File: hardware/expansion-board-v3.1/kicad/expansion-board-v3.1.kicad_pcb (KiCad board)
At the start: 6 copper layers, 100 x 62 mm, 156 parts, among them J1 PinHeader_2x20_P2.54mm_Vertic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, J2 U.FL_Hirose_U.FL-R-SMT-1_Vert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, J4 USB_C_Receptacle_HRO_TYPE-C-3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, J5 U.FL_Hirose_U.FL-R-SMT-1_Vert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, J6 U.FL_Hirose_U.FL-R-SMT-1_Vert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, J8 U.FL_Hirose_U.FL-R-SMT-1_Vert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, Q2 SOT-23, Q3 SOT-23, Q4 SOT-23, Q5 SOT-23, SW1 SolderJumper-2_P1.3mm_Open_Pa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, SW2 SolderJumper-2_P1.3mm_Open_Pa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, U1 SOT-23-5, U10 QFN-48-1EP_7x7mm_P0.5mm_EP5.1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, U11 DFN-8-1EP_2x2mm_P0.5mm_EP0.86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, U12 SOT-363_SC-70-6, U13 AD8319_LFCSP-8-EP, U14 MSOP-8_3x3mm_P0.65mm, U15 SOT-23-6, U16 SOT-363_SC-70-6, U17 SOT-363_SC-70-6, U2 SOT-23-5, U3 SOT-23-5, U4 BNO085_LGA-28, U5 BMP388_LGA-10, U6 LGA-16_3x3mm_P0.5mm, U7 ATGM336H_LCC-18, U8 QFN-56-1EP_7x7mm_P0.4mm_EP3.2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, U9 SOIC-8_5.3x5.3mm_P1.27mm, Y1 Crystal_SMD_3225-4Pin_3.2x2.5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, Y2 Crystal_SMD_3225-4Pin_3.2x2.5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, Y3 Crystal_SMD_3215-2Pin_3.2x1.5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

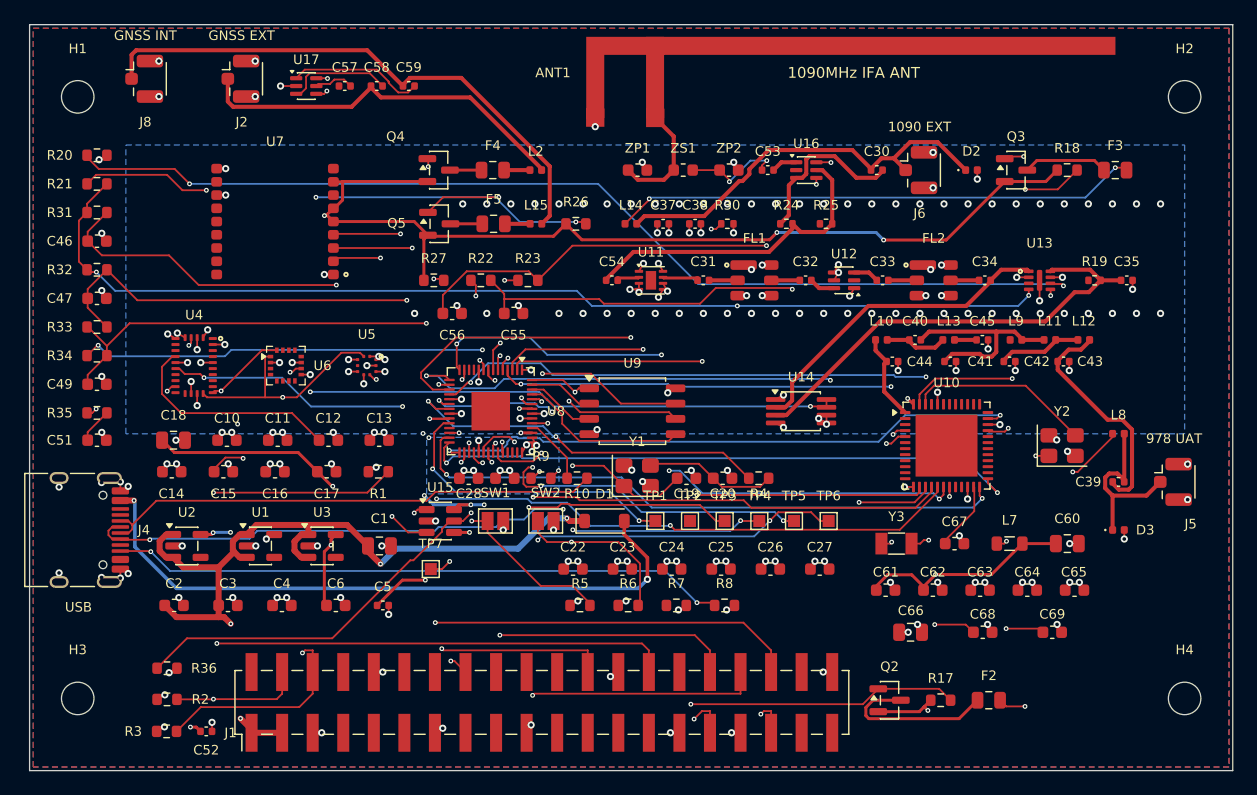
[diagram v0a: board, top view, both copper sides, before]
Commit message: feat(hw): 两脚元件按"最近引脚"定朝向——真缺线 12→4，RF 残线 6→2
评审看图指出的：很多问题不是走线本身，是 L/C 摆放时两个脚的朝向根本没考虑要连
到哪儿去，"很随意就摆了"。结果本该最短的连接反而绕远，还把旁边通道堵死。

查证属实：PLACEMENT.py 里几乎所有 0402 都是 0°，从来没排过朝向。

## orient_opt.py

两脚无极性件（R/L/C）转 180° 电气上等价，但朝向决定走线是短直还是绕过元件本体
再拐回来。判据就是"最近引脚"：

    当前成本 = |pin1 → net1 最近的外部焊盘| + |pin2 → net2 最近的外部焊盘|
    翻转成本 = |pin2位 → net1 最近点|      + |pin1位 → net2 最近点|

只动 ^[RLC]\d+$，二极管等有极性件一律跳过。两脚都是覆铜网（GND/3V3_*/RP_1V1）的
也跳过——那些靠就近过孔入平面，朝向无所谓，算出来的收益是噪声。

选中 25 个，合计省 31.6mm 连线。收益最大的 R21(AD8313_VOUT/RF_DET_OUT) 2.10mm、
R34 2.09mm、C30(ANT1090_EXT/SW1_J2) 1.92mm——C30/C59/R25 正是评审圈出来的那几个。

apply 逐行改 + 断言改了几条，不用大正则套整个文件（PLACEMENT 行内空白对齐不统一，
正则一复杂就静默漏改，项目里栽过这个跟头）。

## 效果（plain 流程，其余条件不变）

                    改朝向前   改朝向后
  freerouting        18         **9** unrouted
  未连通             16         **12**
  真缺线             12 处      **4 处**
  RF 残线            6 条       **2 条**
  铜层 DRC            0          0
  走线/过孔        1318/414   1408/421

只剩 SUBG_RFP / SUBG_RXTX / SUBG_VDDR / I2C_SDA 四处。
check_route 四条硬约束仍全过：In1 参考面完整 / 射频 184 段全在 F.Cu / 射频 0 过孔。

## 还没做的：位置本身摆错的那几个

朝向只能省两脚间距（0.95mm），治不了"元件离目标十几毫米"：
    C57.pin1 GNSS_RF_IN  → 最近同网 U7  12.91mm
    C58.pin1 ANT_GNSS_EXT → 最近同网 J2  11.92mm
    C59.pin1 ANT_GNSS_INT → 最近同网 L15 16.26mm
    L9.pin1  SUBG_RFP    → 最近同网 C44 10.43mm
这几个是 GNSS 天线切换的隔直电容和 balun 电感，内部间距只有 1.8-2.8mm 排得很整齐，
说明摆的时候只顾"这几个排整齐"，没顾它们要连到哪儿。下一步该挪位置，不是转朝向。
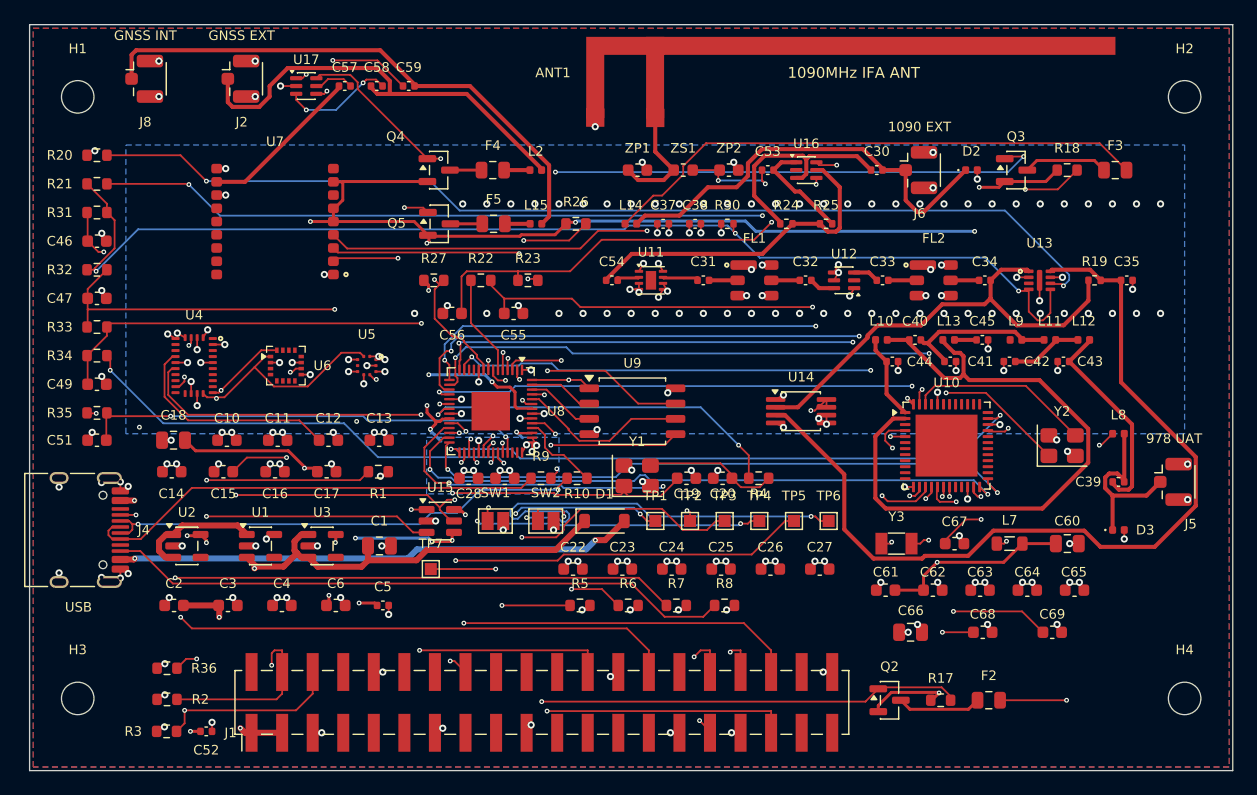
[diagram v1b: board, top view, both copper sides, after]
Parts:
- turned C15 to 180 degrees
- turned C18 to 180 degrees
- turned C2 to 180 degrees
- turned C20 to 180 degrees
- turned C30 to 180 degrees
- turned C42 to 180 degrees
- turned C43 to 180 degrees
- turned C51 to 180 degrees
- turned C56 to 180 degrees
- turned C59 to 180 degrees
- turned C61 to 180 degrees
- turned R1 to 180 degrees
- turned R10 to 180 degrees
- turned R20 to 180 degrees
- turned R21 to 180 degrees
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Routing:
- net USB_CC1: track 0.00 -> 49.7 mm, vias 0 -> 2
- net SUBG_RFN: track 5.21 -> 54.7 mm
- net DET_INLO: track 37.9 -> 73.1 mm
- net RSSI: track 2.93 -> 37.5 mm, vias 0 -> 2
- net SWDIO: track 0.00 -> 29.1 mm, vias 0 -> 3
- net DEMOD2: track 32.0 -> 51.7 mm, vias 4 -> 2
- net GNSS_RF_IN: track 0.00 -> 13.6 mm
- net RP_1V1: track 9.26 -> 21.7 mm, vias 6 -> 7
- net DET_IN: track 26.8 -> 38.4 mm
- net DEMOD3: track 34.4 -> 46.0 mm
- net TL_PWM: track 49.9 -> 38.4 mm, vias 3 -> 2
- net ANT_SEL_GNSS_A: track 56.7 -> 49.0 mm, vias 5 -> 4
- net ADSB_RXD: track 48.0 -> 40.8 mm
- net SUBG_FUSE: track 13.9 -> 7.00 mm
- net SW1_J3: track 2.15 -> 8.87 mm
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
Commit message: feat(hw): 飞线体检工具；未连通 12→11、真缺线 4、铜层 DRC 仅剩 1 项非致命
产品要求："电路板讲求流水，能否通畅就看水管走向歪没歪。原先脚本把所有元件按网格排，
但画 PCB 不是网格是血管，讲求头对脚、脚对头，网格式的头对头脚对脚除了好看一无是处。"

## ratsnest_diag.py —— 把"歪没歪"量化

布线**之前**只看布局，算两个指标：
· 飞线长度：每个网络的最小生成树总长。某条 MST 边特别长 = 这两个焊盘该靠近却
  离得老远，是位置摆错（不是朝向问题，朝向最多差一个元件长）
· 飞线交叉：不同网络的 MST 边互相穿过 = 布局打结，两条线注定抢同一通道

实测暴露的问题（当时）：**飞线总长 2840.9mm、交叉 589 处**，最长的三条是
    DET_TADJ     R20.1(56.4,60.9) ↔ U13.6(134.8,71.5)  79.14mm  横跨整块板
    AD8313_VOUT  U14.8(116.2,81.2) ↔ R21.1(56.4,63.2)  62.44mm
    RF_DET_OUT   R31.1(56.4,65.6) ↔ R30.1(108.5,66.6)  52.09mm
R20/R21/R31 全挤在 x=56.4，而伺候的 U13/U14 在 x=108~135。

病根在 gen_pcb.py:83/88：区域装箱装不下就溢出到 "LEFT_EDGE 左边缘空地"，
装箱只关心塞得下，完全不管这元件要连到哪儿。R20 因此违反 §2.5「RTADJ 紧贴引脚」。

## replace_opt.py —— 归位尝试，结论是**先别用**

按"连接重心"算每个元件该在哪，挪了 24 个：飞线 2840.9→2396.5mm(-15.6%)、
交叉 589→518。看着漂亮，实际布完 **24 条 courtyards_overlap + 8 条 shorting_items**
——判空位用的是"焊盘范围+1.2mm"，而 KiCad 判重叠看的是 **courtyard(元件外框)**，
比焊盘大一圈，挪出来的"空位"全是压在别人身上的假空位。已回退。

工具已改用 courtyard + 0.2mm 呼吸位重判。改完只剩 3 个能挪（L14/R30/L15），
其中两个还是射频偏置电感——板子本来就挤，归位空间有限，收益不抵风险，暂不启用。
留着工具和这段教训。

两个附带教训：
· 算重心只能用**小网络**（≤6 焊盘）。大电源网取平均没有物理意义，去耦电容会被
  从"贴着芯片脚"挪到板子中间，正好挪反
· 跑流程要**每步验板子非空**。这轮有一次跑完板子变成 623KB/0 走线的空板，一路
  跑到验收才发现（元凶未查明，怀疑并发的 freerouting 进程），白跑一轮

## 当前状态（历史最好）

              e917f2a   e72e6cd   本次
  未连通         16        12      **11**
  真缺线         12         4        4
  铜层 DRC        0         0     1(非致命)
  射频        156段      184段    189段 全F.Cu / 0过孔

剩的 1 项铜层 DRC 是 SW2.pad2(GND) 热焊盘辐条 1 条（板规要求 2）——不是断路，
1 条辐条照样导通，只是焊接散热略差，打样可接受。
真缺线 4 处：SUBG_RXTX / SUBG_X48N / I2C_SDA / DEMOD3。
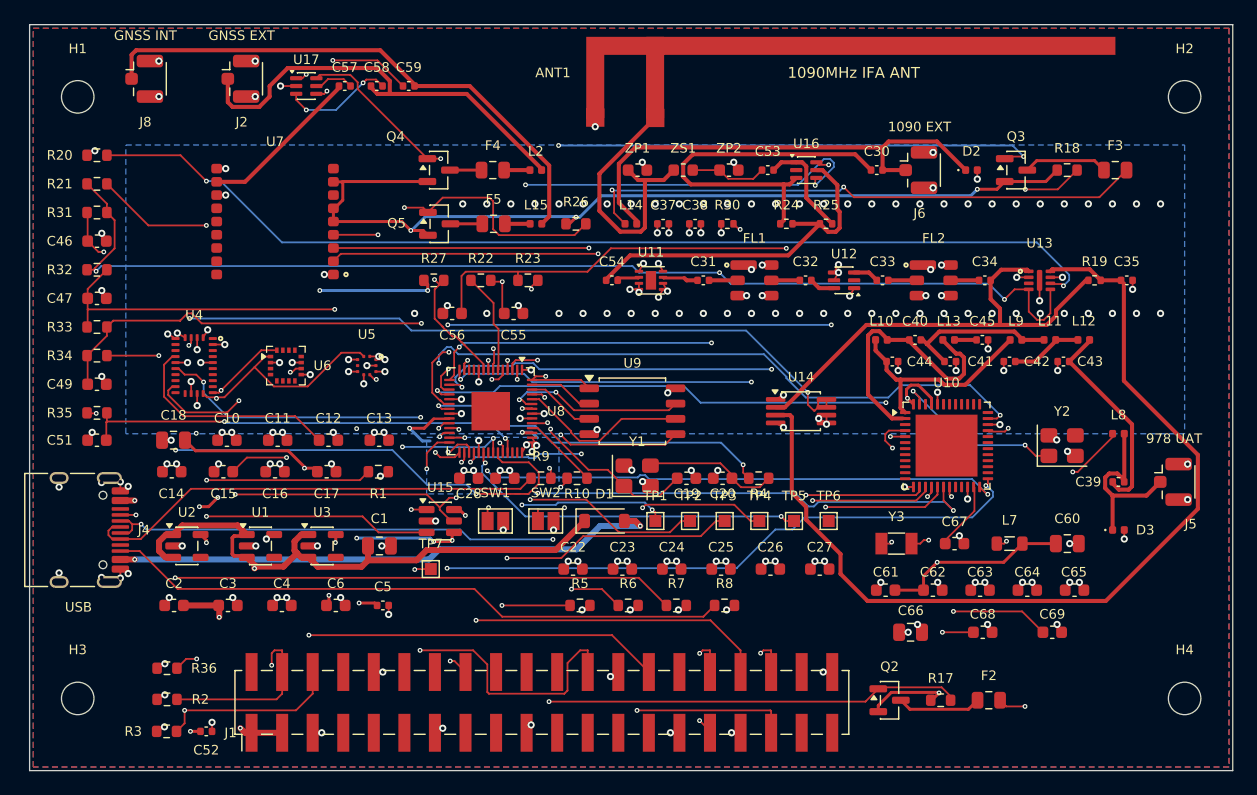
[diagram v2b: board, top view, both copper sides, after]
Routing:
- net DEMOD3: track 46.0 -> 0.00 mm, vias 3 -> 0
- net SUBG_RFN: track 54.7 -> 22.6 mm
- net DEMOD2: track 51.7 -> 29.5 mm
- net SUBG_X48N: track 15.2 -> 0.00 mm
- net ANT1090_IFA: track 9.45 -> 22.7 mm
- net SUBG_RESET: track 49.4 -> 62.1 mm, vias 2 -> 3
- net SW1_J2: track 18.7 -> 30.8 mm
- net TL_PWM: track 38.4 -> 50.2 mm, vias 2 -> 3
- net SUBG_RFP: track 7.06 -> 18.1 mm
- net SUBG_TCKC: track 51.3 -> 62.2 mm, vias 2 -> 3
- net SUBG_CSN: track 58.8 -> 52.9 mm
- net IMU_INT: track 65.1 -> 59.4 mm
- net RECOVERED_CLK: track 15.3 -> 21.0 mm, vias 2 -> 3
- net BARO_INT: track 40.5 -> 46.1 mm
- net 3V3_GNSS: track 177.7 -> 183.2 mm, vias 10 -> 9
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
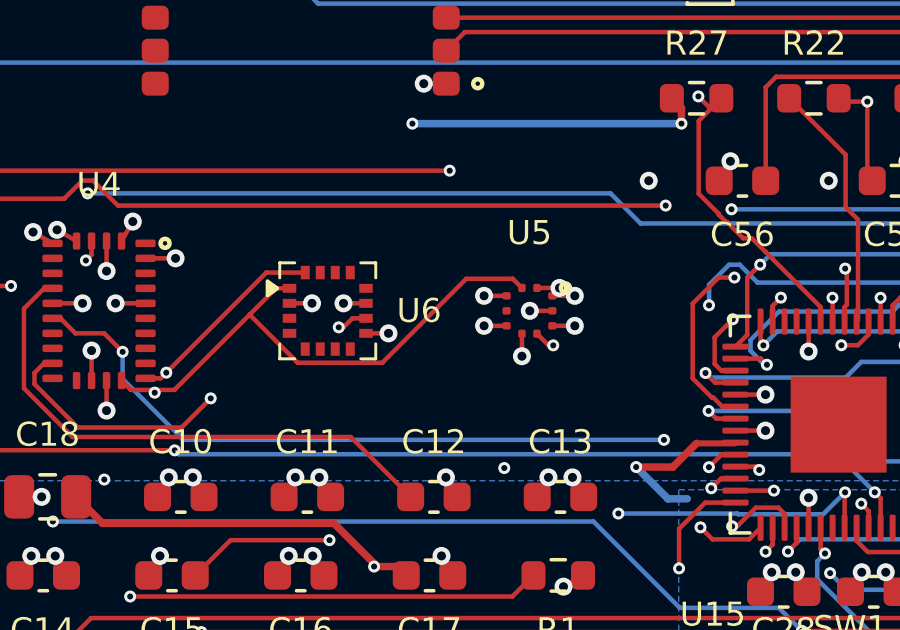
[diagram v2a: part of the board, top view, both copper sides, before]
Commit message: fix(hw): 挡路的是 GND 缝合过孔不是信号线——删 2 个，I2C_SDA 通了，真缺线 4→3
评审看图判断"还是可解的"，查证属实，但可解的原因和我先前判断的不一样。

## 挡路者盘点（route_fix 点名 + 连续几何算余量）

  SUBG_X48N   缺口 11.80mm  挡：SUBG_VDDR 走线      余量 **+0.227mm**
  I2C_SDA     缺口  6.68mm  挡：GND 走线/过孔       余量 **+0.114mm**
  DEMOD3      缺口 28.19mm  挡：DEMOD2 过孔         余量 **+0.067mm**
  SUBG_RXTX   缺口  7.51mm  挡：SUBG_RFN 走线       余量 **-0.181mm**

前三条余量是**正的**——几何上过得去，是 route_fix 的 0.15mm 栅格抓不住
0.07~0.23mm 的窄窗口。所以把 route_rf_manual（0.05mm 栅格）从"只认射频"扩展成
能点名任意网络，线宽按网络类自动取（RF50 才 0.34，Default 是 0.15）。

## 但 0.05mm 栅格也不够，占用图看出真凶

SUBG_X48N 只扩展 1020 节点就无解。打出它周围的占用图：起点被困在一个
**3 格宽、y 只有 81.04~82.14 的小格子**里，四周全封死。挡路者第一名是
**GND 375 格**——route_rf.py 撒的 183 个平面缝合过孔 + 53 个栅栏过孔，
把 U10 的引脚出口堵死了。

GND 过孔是**可以删**的：它靠平面连通，route_rf.py 自己就说"5 个焊盘无空位、
靠覆铜连接"。删两个不影响接地。

## ripup_retry.py

按 route_fix 的 ripup.json 精确拆指定走线/过孔（net + 层 + 端点坐标匹配，
容差 0.01mm）。跟"全局 rip-up"的区别是只拆明确点名的挡路者，拆一条布两条，
用**未连通总数**验收，不赚就整体回退。

两次实测：
· 拆 6 项信号线（DEMOD2/SUBG_TMSC/SUBG_VDDR + GND）→ 未连通 11→**13**、
  铜层 DRC 1→6。补上 I2C_SDA 一条，但拆掉的三条都没布回来。**已回退**，
  再次印证自研 A* 重布不回 freerouting 的原布法
· 只删 2 个 GND 缝合过孔 (76.51,77.84) 和 (76.51,78.84) → 未连通不变 11
  （GND 毫发无损），再用 0.05mm 栅格布 I2C_SDA → **通了**（11 折 17.95mm）

## 结果

              上一版   本次
  未连通        11     **10**
  真缺线         4      **3**
  铜层 DRC     1(非致命) 1(非致命，SW2 热焊盘辐条)
  射频        189段    188段 全 F.Cu / 0 过孔

剩 3 条及其性质：
· SUBG_X48N  被 SUBG_VDDR 挡，删 GND 过孔救不了（试过），需要动 VDDR 走线或换层
· DEMOD3     被 DEMOD2 过孔挡，删了 DEMOD2 就得重布它，风险高
· SUBG_RXTX  余量 **-0.181mm**，现在就是负的，纯几何不可解，必须改布局
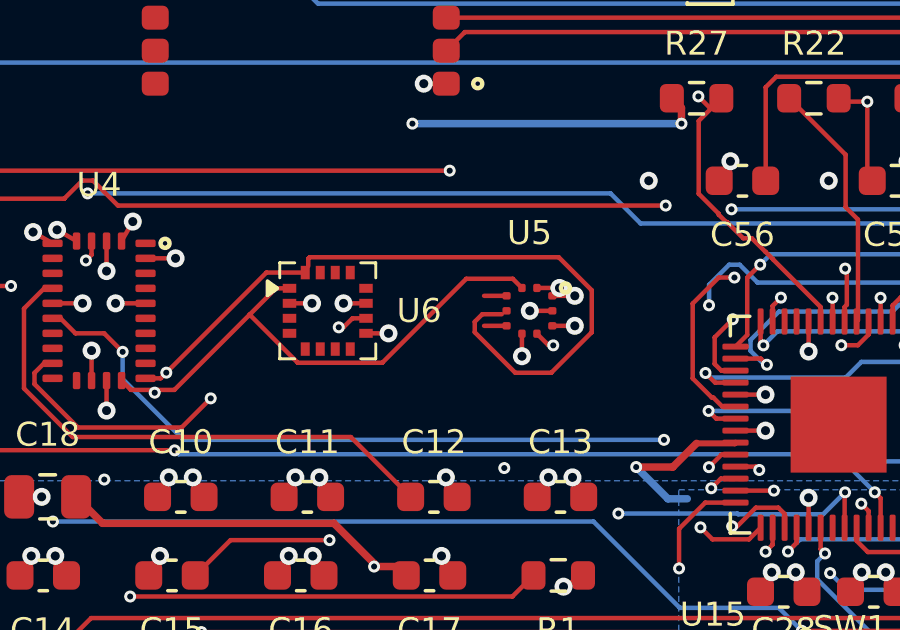
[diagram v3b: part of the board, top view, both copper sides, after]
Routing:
- net I2C_SDA: track 45.9 -> 63.8 mm
- net GND: vias 186 -> 184
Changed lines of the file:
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@@
 	)
 	(via
-		(at 76.5105 77.836)
-		(size 0.6)
-		(drill 0.3)
-		(layers "F.Cu" "B.Cu")
-		(net "GND")
-	)
-	(via
 		(at 96 64.9)
 		(size 0.6)
@@
 	)
 	(via
-		(at 76.5105 78.836)
-		(size 0.6)
-		(drill 0.3)
-		(layers "F.Cu" "B.Cu")
-		(net "GND")
-	)
-	(via
 		(at 134 74)
 		(size 0.6)
@@
 	)
 	(segment
+		(start 77.55 80.4)
+		(end 76.2 79.05)
+		(width 0.15)
+		(layer "F.Cu")
+		(net "I2C_SDA")
+	)
+	(segment
 		(start 70.99 102.0033)
 		(end 70.3541 102.0033)
@@
 	)
 	(segment
+		(start 76.2 78.7)
+		(end 76.45 78.45)
+		(width 0.15)
+		(layer "F.Cu")
+		(net "I2C_SDA")
+	)
+	(segment
+		(start 78.75 80.4)
+		(end 77.55 80.4)
+		(width 0.15)
+		(layer "F.Cu")
+		(net "I2C_SDA")
+	)
+	(segment
+		(start 80.1 77.65)
+		(end 80.1 79.05)
+		(width 0.15)
+		(layer "F.Cu")
+		(net "I2C_SDA")
+	)
+	(segment
+		(start 76.2 79.05)
+		(end 76.2 78.7)
+		(width 0.15)
+		(layer "F.Cu")
+		(net "I2C_SDA")
+	)
+	(segment
+		(start 80.1 79.05)
+		(end 78.75 80.4)
+		(width 0.15)
+		(layer "F.Cu")
+		(net "I2C_SDA")
+	)
+	(segment
+		(start 70.65 76.85)
+		(end 70.65 76.6)
+		(width 0.15)
+		(layer "F.Cu")
+		(net "I2C_SDA")
+	)
+	(segment
 		(start 70.1225 102.2349)
 		(end 70.1225 103.2435)
@@
 	)
 	(segment
+		(start 70.65 76.6)
+		(end 70.7 76.55)
+		(width 0.15)
+		(layer "F.Cu")
+		(net "I2C_SDA")
+	)
+	(segment
+		(start 79 76.55)
+		(end 80.1 77.65)
+		(width 0.15)
+		(layer "F.Cu")
+		(net "I2C_SDA")
+	)
+	(segment
 		(start 65.9184 80.397)
 		(end 69.2544 77.061)
 		(width 0.15)
 		(layer "F.Cu")
+		(net "I2C_SDA")
+	)
+	(segment
+		(start 76.45 78.45)
+		(end 77.1 78.45)
+		(width 0.15)
+		(layer "F.Cu")
+		(net "I2C_SDA")
+	)
+	(segment
+		(start 70.7 76.55)
+		(end 79 76.55)
+		(width 0.15)
+		(layer "F.Cu")

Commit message: feat(hw): via-in-pad 解开 SUBG_X48N——真缺线 3→2，未连通 10→9
评审提问"via-in-pad 不行吗"。行，是我先前用错了尺寸。

## 几何核算（0.5mm pitch QFN，焊盘 0.25×0.875mm）

相邻焊盘边缘间距 = 0.5 − 0.25 = 0.25mm，盘超出焊盘的部分要吃掉它：

  盘0.4/孔0.2(当时板规)  超出每侧0.075 → 到邻居 0.100mm < 0.15  ❌
  盘0.3/孔0.15           超出每侧0.025 → 到邻居 0.200mm，环宽 0.075  ✅ 两项都有裕度
  盘0.25/孔0.15          不超出        → 到邻居 0.250mm，环宽 0.050  ⚠️ 环宽=JLC下限，零裕度

选 0.3/0.15。板规的 min_via_diameter 0.4→0.3、min_via_annular_width 0.1→0.075、
min_through_hole 0.2→0.15（都是下限，0.4mm 的常规过孔照旧）。
⚠️ 依赖嘉立创的树脂塞孔+电镀盖帽，6 层及以上默认标配（官网已核），不额外收费。

## 挡路的是 B.Cu，不是邻居焊盘

第一次放完直接 shorting：via-in-pad 是**通孔，穿到 B.Cu**，而 SUBG_X48P 有条
6.35mm 斜线正好从下面过，距离 0.047mm。焊盘长 0.875mm，两端都试过，最远也只有
0.3mm，而需要 0.15+0.075+0.15=0.375mm——放哪都撞。

所以先拆掉 X48P 那段 B.Cu 线，放 via-in-pad，再让 0.05mm 精修器把两条都布出来：
  SUBG_X48N  2 折 12.76mm / 1 过孔（从 via-in-pad 下到 B.Cu 走出去）
  SUBG_X48P  3 折 6.77mm  / 0 过孔（原路补回）
最后一条 clearance 是新走线蹭到 GND 缝合过孔，只差 0.012mm（0.138 vs 0.150），
删掉那个过孔即可——GND 靠平面，前面已验证删缝合过孔不影响连通。

## ⚠️ KiCad 9 的层号编码变了

手写 ripup 清单时按老编码填 B.Cu=31，怎么都匹配不上。实际这版是：
    F_Cu=0  B_Cu=2  In1=4  In2=6  In3=8  In4=10
（不是传统的 F=0/In1..In30/B=31）。工具里凡是用 pcbnew.B_Cu 常量的都没事，
**只有手写数字的地方会中招**。

## 现状

              上一版   本次
  未连通        10     **9**
  真缺线         3     **2**
  铜层 DRC   1(非致命) 1(非致命，SW2 热焊盘辐条)
  走线/过孔  1443/420  1447/421   射频 188 段全 F.Cu / 0 过孔

剩 2 处：
· DEMOD3     缺口 28mm，多层能算出路径但过不了 KiCad clearance（复核缺覆铜）
· SUBG_RXTX  余量 −0.181mm，射频不能打孔绕，纯几何不可解 → 只能改布局
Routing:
- net SUBG_X48N: track 0.00 -> 12.8 mm, vias 0 -> 2
- net GND: vias 184 -> 183
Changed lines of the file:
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@@
 	)
 	(via
-		(at 135.368 84.513)
-		(size 0.6)
-		(drill 0.3)
-		(layers "F.Cu" "B.Cu")
-		(net "GND")
-	)
-	(via
 		(at 112 64.9)
 		(size 0.6)
@@
 		(net "SUBG_RESET")
 	)
+	(via
+		(at 136.2 84)
+		(size 0.4)
+		(drill 0.2)
+		(layers "F.Cu" "B.Cu")
+		(net "SUBG_X48N")
+	)
+	(via
+		(at 124.462 81.55)
+		(size 0.3)
+		(drill 0.15)
+		(layers "F.Cu" "B.Cu")
+		(net "SUBG_X48N")
+	)
+	(segment
+		(start 126.9 84)
+		(end 136.2 84)
+		(width 0.15)
+		(layer "B.Cu")
+		(net "SUBG_X48N")
+	)
+	(segment
+		(start 124.45 81.55)
+		(end 126.9 84)
+		(width 0.15)
+		(layer "B.Cu")
+		(net "SUBG_X48N")
+	)
 	(segment
 		(start 133.6273 85.838)
@@
 	)
 	(segment
+		(start 127.25 84.95)
+		(end 127.95 84.95)
+		(width 0.15)
+		(layer "B.Cu")
+		(net "SUBG_X48P")
+	)
+	(segment
+		(start 123.45 80.45)
+		(end 123.45 81.15)
+		(width 0.15)
+		(layer "B.Cu")
+		(net "SUBG_X48P")
+	)
+	(segment
 		(start 127.9268 84.9483)
 		(end 132.7376 84.9483)
@@
 	)
 	(segment
-		(start 123.4365 80.458)
-		(end 127.9268 84.9483)
+		(start 123.45 81.15)
+		(end 127.25 84.95)
 		(width 0.15)
 		(layer "B.Cu")
